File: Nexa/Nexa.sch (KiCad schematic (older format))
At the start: 75 parts, among them J1 Conn_01x04, J10 Conn_01x02_Male, J11 DB9_Female, J12 Conn_01x02_Male, J13 Conn_01x02_Male, J14 Conn_01x01, J15 Conn_01x01, J16 Conn_01x01, J17 Conn_01x01, J18 Conn_01x01, J19 Conn_01x01, J2 Conn_01x02_Male, J20 Conn_01x01, J21 Conn_01x01, J3 Conn_01x04, J4 Conn_02x03_Odd_Even, J5 Conn_01x23, J6 proto_grid_15x21, J7 Conn_02x02_Top_Bottom, J8 Conn_02x02_Top_Bottom, J9 Conn_01x02_Male, Q1 Q_NMOS_DGS, SW1 SW_Push, U1 STM32F103C8, U2 LM1117-5.0, U3 LM1117-3.3, U4 MAX485E, U5 MAX485E, Y1 8 MHz, Y2 32.768 KHz

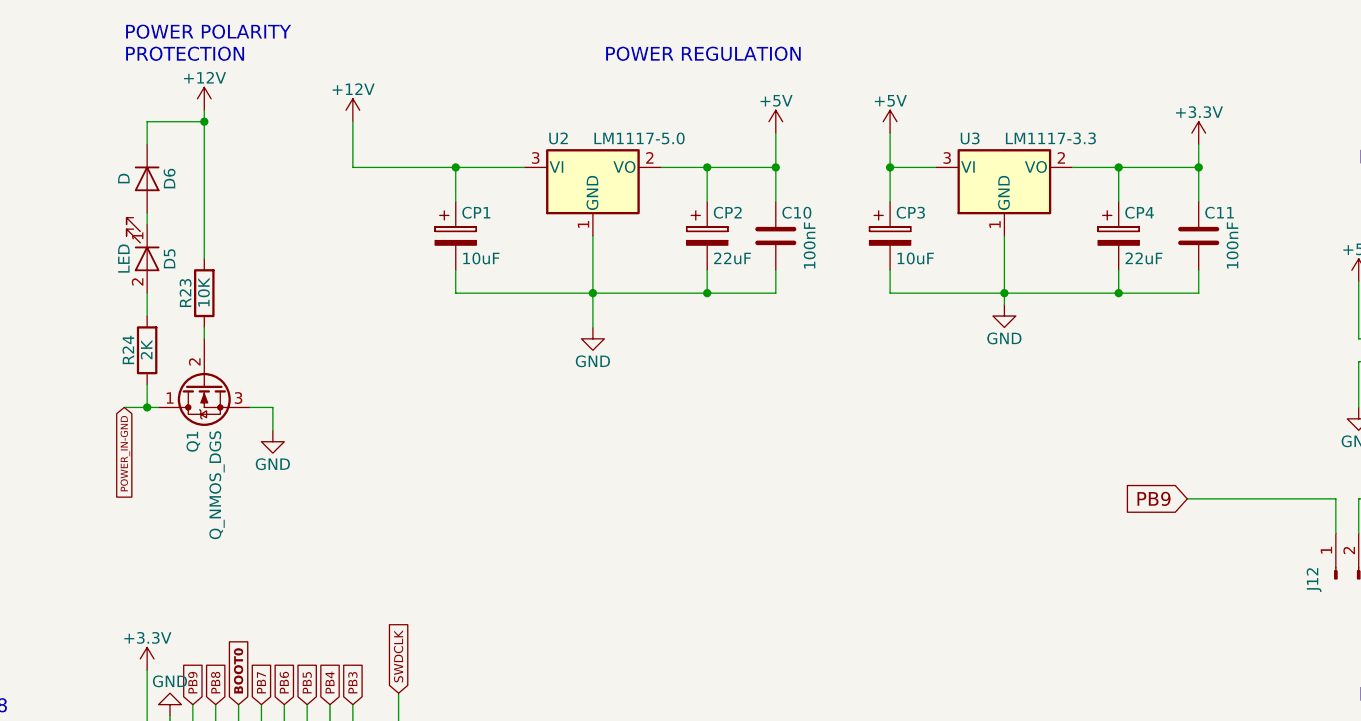
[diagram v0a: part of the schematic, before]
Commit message: Issue #1 and #2 closed
#1 Polarity protection N_Mosfet is NOT correct configured
Mosfets had incorrect pinout.
#2 CP1 (10nF-16V), max V should be oversize
CP1 is now a 25V cap
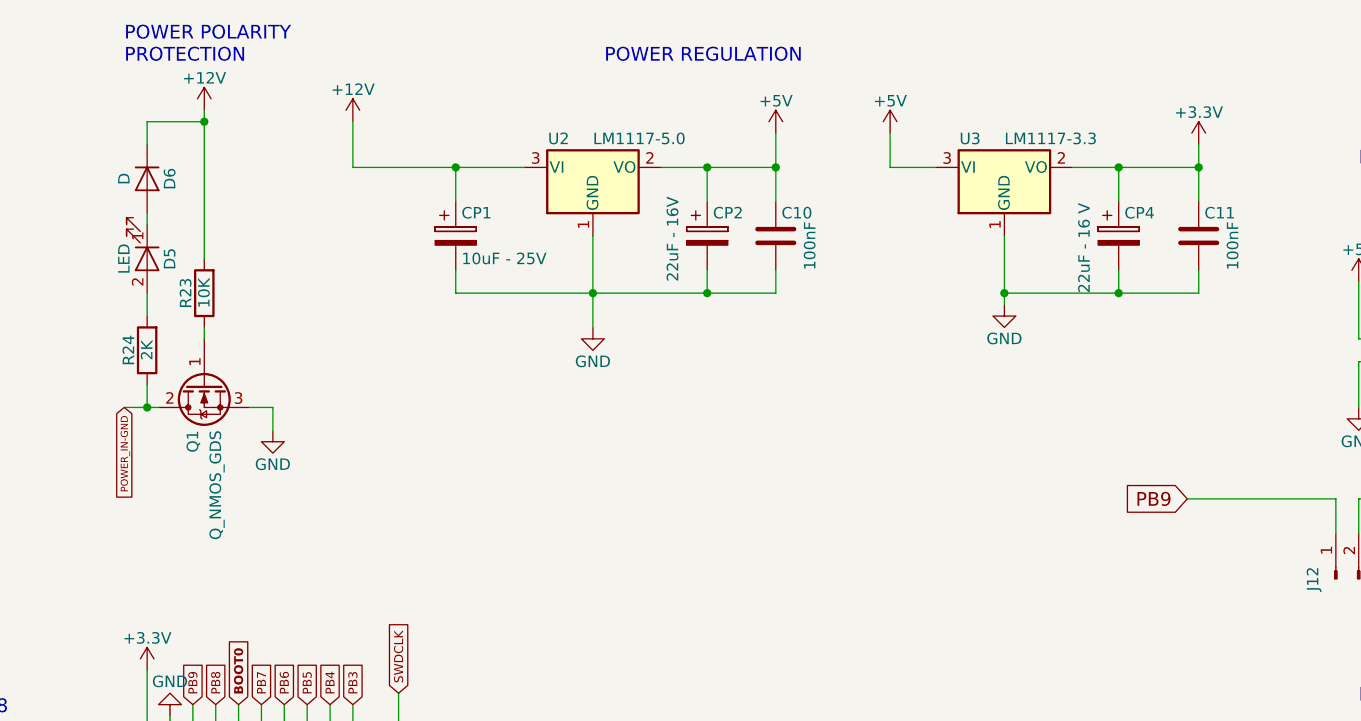
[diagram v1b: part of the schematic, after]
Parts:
- removed CP3: 10uF, Capacitors_Tantalum_SMD:CP_Tantalum_Case-B_EIA-3528-21_Hand, symbol CP
- removed Q1: Q_NMOS_DGS, TO_SOT_Packages_SMD:TO-252-2, symbol Q_NMOS_DGS
- added Q1: Q_NMOS_GDS, TO_SOT_Packages_SMD:TO-252-2, symbol Q_NMOS_GDS
- CP1: value 10uF -> 10uF - 25V; footprint Capacitors_Tantalum_SMD:CP_Tantalum_Case-B_EIA-3528-21_Hand -> Capacitors_Tantalum_SMD:CP_Tantalum_Case-C_EIA-6032-28_Hand
- CP2: value 22uF -> 22uF - 16V
- CP4: value 22uF -> 22uF - 16 V
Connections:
- net GND: now also Q1.3 (S)
- net POWER_IN-GND: now also Q1.2 (D)
- net at R23.1: now also Q1.1 (G)
